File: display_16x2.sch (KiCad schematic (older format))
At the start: 1 part

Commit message: reorganized schematic; added reverse polarity protection; start adding footprints
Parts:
- removed DS1: HY1602E, Display:HY1602E, symbol Display_Character:HY1602E
- added DS1: WC1602A, Display:WC1602A, symbol Display_Character:WC1602A
- added R?: R, symbol Device:R
- added RV?: R_POT, symbol Device:R_POT
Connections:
- net labels added: +5V, D4, D5, D6, D7, E, GND, RS
- wire segments 0 -> 14
- no-connect marks 0 -> 4
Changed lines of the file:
@@
 $Descr A4 11693 8268
 encoding utf-8
-Sheet 7 7
+Sheet 7 9
 Title "PUTM_EV_Dashboard_2021"
 Date ""
@@
 $EndDescr
 $Comp
-L Display_Character:HY1602E DS1
-U 1 1 5FBBC8BA
-P 4600 3900
-F 0 "DS1" H 4600 4881 50  0000 C CNN
-F 1 "HY1602E" H 4600 4790 50  0000 C CNN
-F 2 "Display:HY1602E" H 4600 3000 50  0001 C CIN
-F 3 "http://www.icbank.com/data/ICBShop/board/HY1602E.pdf" H 4800 4000 50  0001 C CNN
-	1    4600 3900
+L Device:R_POT RV?
+U 1 1 620FC9A3
+P 5550 2750
+F 0 "RV?" H 5480 2704 50  0000 R CNN
+F 1 "R_POT" H 5480 2795 50  0000 R CNN
+F 2 "" H 5550 2750 50  0001 C CNN
+F 3 "~" H 5550 2750 50  0001 C CNN
+	1    5550 2750
+	-1   0    0    1
+$EndComp
+$Comp
+L Display_Character:WC1602A DS1
+U 1 1 620FE188
+P 4600 3350
+F 0 "DS1" H 4400 4100 50  0000 C CNN
+F 1 "WC1602A" H 4800 4100 50  0000 C CNN
+F 2 "Display:WC1602A" H 4600 2450 50  0001 C CIN
+F 3 "http://www.wincomlcd.com/pdf/WC1602A-SFYLYHTC06.pdf" H 5300 3350 50  0001 C CNN
+	1    4600 3350
 	1    0    0    -1
 $EndComp
+$Comp
+L power:GND #PWR?
+U 1 1 62101DBF
+P 4600 4150
+F 0 "#PWR?" H 4600 3900 50  0001 C CNN
+F 1 "GND" H 4605 3977 50  0000 C CNN
+F 2 "" H 4600 4150 50  0001 C CNN
+F 3 "" H 4600 4150 50  0001 C CNN
+	1    4600 4150
+	1    0    0    -1
+$EndComp
+Wire Wire Line
+	5000 2750 5400 2750
+$Comp
+L power:GND #PWR?
+U 1 1 62102476
+P 5550 3200
+F 0 "#PWR?" H 5550 2950 50  0001 C CNN
+F 1 "GND" H 5555 3027 50  0000 C CNN
+F 2 "" H 5550 3200 50  0001 C CNN
+F 3 "" H 5550 3200 50  0001 C CNN
+	1    5550 3200
+	1    0    0    -1
+$EndComp
+$Comp
+L Device:R R?
+U 1 1 621030E4
+P 5150 2500
+F 0 "R?" H 5220 2546 50  0000 L CNN
+F 1 "R" H 5220 2455 50  0000 L CNN
+F 2 "" V 5080 2500 50  0001 C CNN
+F 3 "~" H 5150 2500 50  0001 C CNN
+	1    5150 2500
+	1    0    0    -1
+$EndComp
+$Comp
+L power:+5V #PWR?
+U 1 1 62103E40
+P 5150 2200
+F 0 "#PWR?" H 5150 2050 50  0001 C CNN
+F 1 "+5V" H 5165 2373 50  0000 C CNN
+F 2 "" H 5150 2200 50  0001 C CNN
+F 3 "" H 5150 2200 50  0001 C CNN
+	1    5150 2200
+	1    0    0    -1
+$EndComp
+Wire Wire Line
+	5000 3050 5150 3050
+Wire Wire Line
+	5150 2200 5150 2250
+Wire Wire Line
+	5150 2650 5150 3050
+Wire Wire Line
+	4600 2550 4600 2250
+Wire Wire Line
+	4600 2250 5150 2250
+Connection ~ 5150 2250
+Wire Wire Line
+	5150 2250 5150 2350
+Wire Wire Line
+	5150 2250 5550 2250
+Wire Wire Line
+	5550 2250 5550 2600
+Wire Wire Line
+	5000 3150 5550 3150
+Wire Wire Line
+	5550 3200 5550 3150
+Wire Wire Line
+	5550 3150 5550 2900
+Connection ~ 5550 3150
+NoConn ~ 4200 3250
+NoConn ~ 4200 3350
+NoConn ~ 4200 3450
+NoConn ~ 4200 3550
+Text HLabel 4200 3650 0    50   Input ~ 0
+D4
+Text HLabel 4200 3750 0    50   Input ~ 0
+D5
+Text HLabel 4200 3850 0    50   Input ~ 0
+D6
+Text HLabel 4200 3950 0    50   Input ~ 0
+D7
+Wire Wire Line
+	4200 2850 3900 2850
+Wire Wire Line
+	3900 2850 3900 3050
+$Comp
+L power:GND #PWR?
+U 1 1 6210717D
+P 3900 3050
+F 0 "#PWR?" H 3900 2800 50  0001 C CNN
+F 1 "GND" H 3905 2877 50  0000 C CNN
+F 2 "" H 3900 3050 50  0001 C CNN
+F 3 "" H 3900 3050 50  0001 C CNN
+	1    3900 3050
+	1    0    0    -1
+$EndComp
+Text HLabel 4200 2750 0    50   Input ~ 0
+E
+Text HLabel 4200 2950 0    50   Input ~ 0
+RS
 $EndSCHEMATC

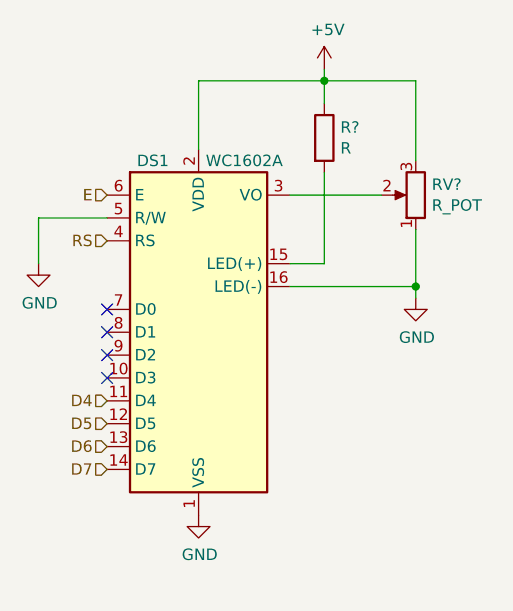
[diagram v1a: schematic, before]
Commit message: footprints; library for 7seg; start pcb layout
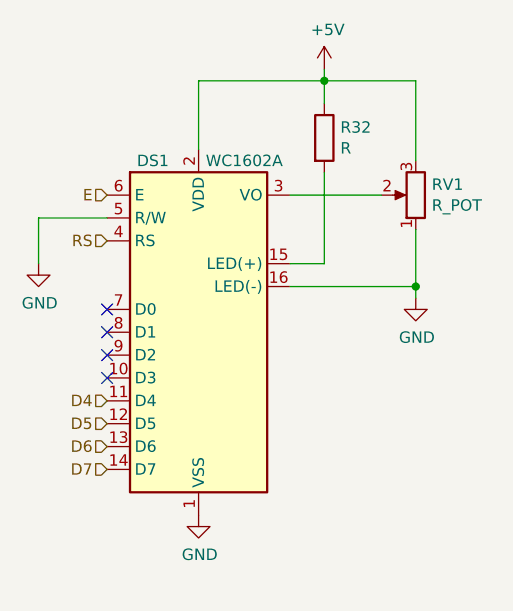
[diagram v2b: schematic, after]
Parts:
- R32: renamed from R?; footprint (none) -> Resistor_SMD:R_0603_1608Metric
- RV1: renamed from RV?; footprint (none) -> Potentiometer_SMD:Potentiometer_Vishay_TS53YJ_Vertical
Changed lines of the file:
@@
 $Descr A4 11693 8268
 encoding utf-8
-Sheet 7 9
+Sheet 5 9
 Title "PUTM_EV_Dashboard_2021"
 Date ""
@@
 $EndDescr
 $Comp
-L Device:R_POT RV?
+L Device:R_POT RV1
 U 1 1 620FC9A3
 P 5550 2750
-F 0 "RV?" H 5480 2704 50  0000 R CNN
+F 0 "RV1" H 5480 2704 50  0000 R CNN
 F 1 "R_POT" H 5480 2795 50  0000 R CNN
-F 2 "" H 5550 2750 50  0001 C CNN
+F 2 "Potentiometer_SMD:Potentiometer_Vishay_TS53YJ_Vertical" H 5550 2750 50  0001 C CNN
 F 3 "~" H 5550 2750 50  0001 C CNN
 	1    5550 2750
@@
 $EndComp
 $Comp
-L power:GND #PWR?
+L power:GND #PWR037
 U 1 1 62101DBF
 P 4600 4150
-F 0 "#PWR?" H 4600 3900 50  0001 C CNN
+F 0 "#PWR037" H 4600 3900 50  0001 C CNN
 F 1 "GND" H 4605 3977 50  0000 C CNN
 F 2 "" H 4600 4150 50  0001 C CNN
@@
 	5000 2750 5400 2750
 $Comp
-L power:GND #PWR?
+L power:GND #PWR039
 U 1 1 62102476
 P 5550 3200
-F 0 "#PWR?" H 5550 2950 50  0001 C CNN
+F 0 "#PWR039" H 5550 2950 50  0001 C CNN
 F 1 "GND" H 5555 3027 50  0000 C CNN
 F 2 "" H 5550 3200 50  0001 C CNN
@@
 $EndComp
 $Comp
-L Device:R R?
+L Device:R R32
 U 1 1 621030E4
 P 5150 2500
-F 0 "R?" H 5220 2546 50  0000 L CNN
+F 0 "R32" H 5220 2546 50  0000 L CNN
 F 1 "R" H 5220 2455 50  0000 L CNN
-F 2 "" V 5080 2500 50  0001 C CNN
+F 2 "Resistor_SMD:R_0603_1608Metric" V 5080 2500 50  0001 C CNN
 F 3 "~" H 5150 2500 50  0001 C CNN
 	1    5150 2500
@@
 $EndComp
 $Comp
-L power:+5V #PWR?
+L power:+5V #PWR038
 U 1 1 62103E40
 P 5150 2200
-F 0 "#PWR?" H 5150 2050 50  0001 C CNN
+F 0 "#PWR038" H 5150 2050 50  0001 C CNN
 F 1 "+5V" H 5165 2373 50  0000 C CNN
 F 2 "" H 5150 2200 50  0001 C CNN
@@
 	3900 2850 3900 3050
 $Comp
-L power:GND #PWR?
+L power:GND #PWR036
 U 1 1 6210717D
 P 3900 3050
-F 0 "#PWR?" H 3900 2800 50  0001 C CNN
+F 0 "#PWR036" H 3900 2800 50  0001 C CNN
 F 1 "GND" H 3905 2877 50  0000 C CNN
 F 2 "" H 3900 3050 50  0001 C CNN

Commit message: Hardware update Approved
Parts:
- R32: value R -> 0R
- RV1: value R_POT -> 10k
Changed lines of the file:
@@
 EESchema Schematic File Version 4
+LIBS:dash_hw-cache
 EELAYER 30 0
 EELAYER END
@@
 P 5550 2750
 F 0 "RV1" H 5480 2704 50  0000 R CNN
-F 1 "R_POT" H 5480 2795 50  0000 R CNN
+F 1 "10k" H 5480 2795 50  0000 R CNN
 F 2 "Potentiometer_SMD:Potentiometer_Vishay_TS53YJ_Vertical" H 5550 2750 50  0001 C CNN
 F 3 "~" H 5550 2750 50  0001 C CNN
@@
 P 5150 2500
 F 0 "R32" H 5220 2546 50  0000 L CNN
-F 1 "R" H 5220 2455 50  0000 L CNN
+F 1 "0R" H 5220 2455 50  0000 L CNN
 F 2 "Resistor_SMD:R_0603_1608Metric" V 5080 2500 50  0001 C CNN
 F 3 "~" H 5150 2500 50  0001 C CNN
